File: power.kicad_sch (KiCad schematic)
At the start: 37 parts, among them Q2 BSS138-7-F, Q3 BSS138-7-F, U1 TPS56C230, U6 74AUP2G132

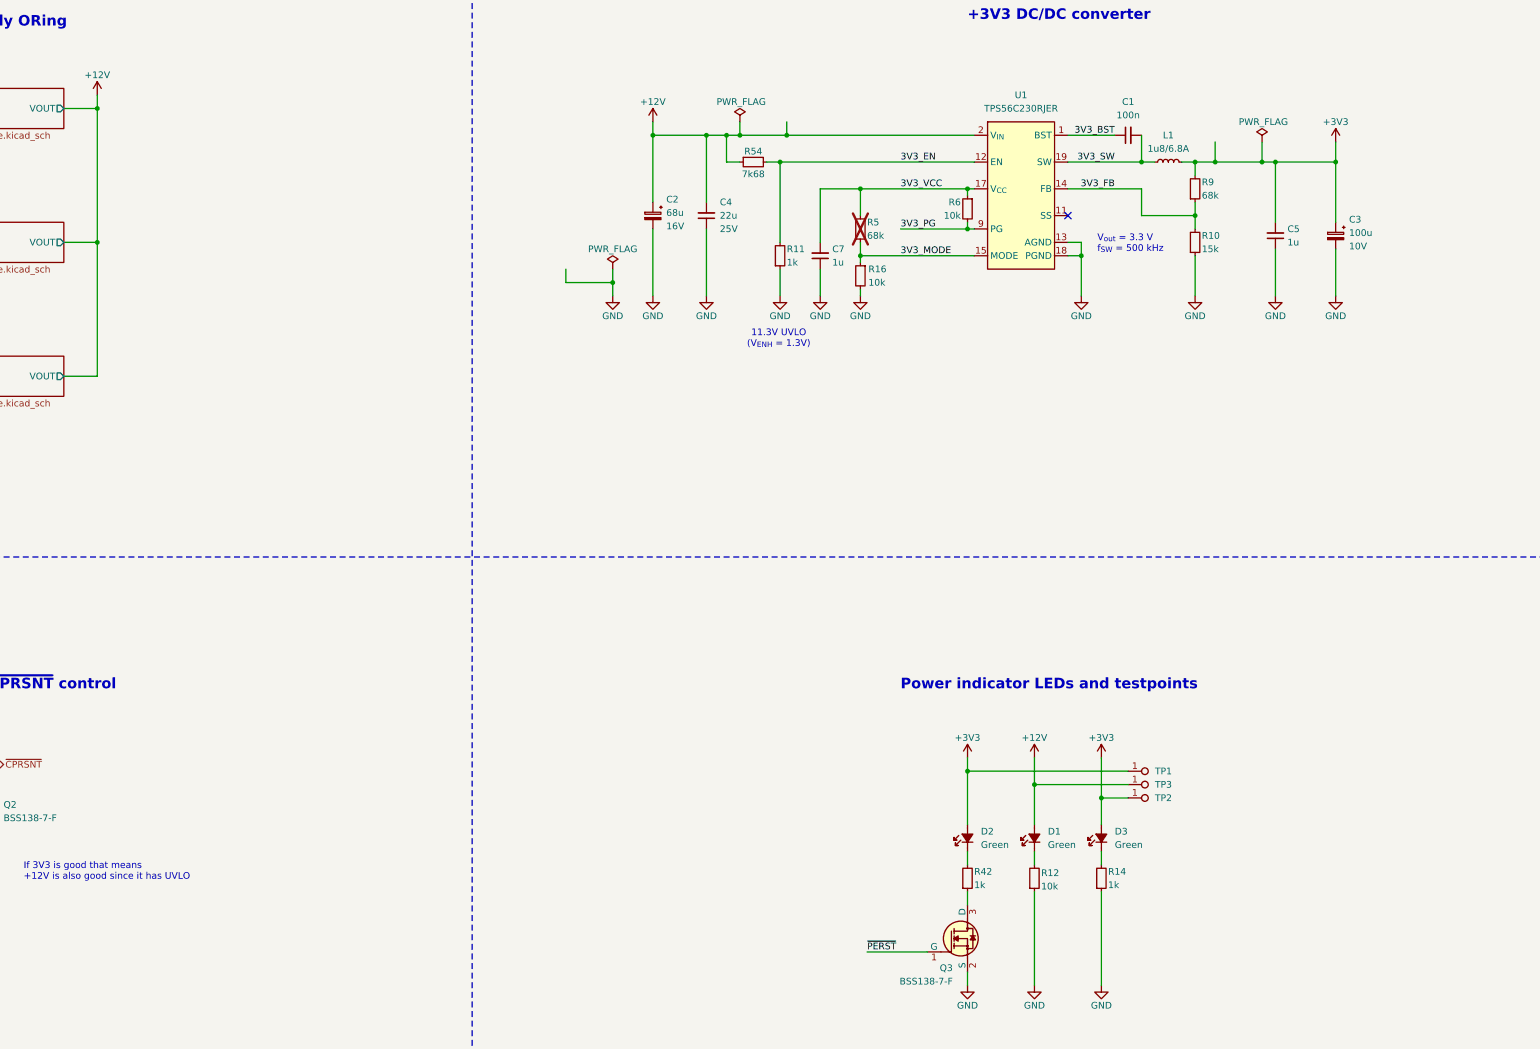
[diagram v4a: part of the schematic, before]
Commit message: [#79262] Route high speed and power
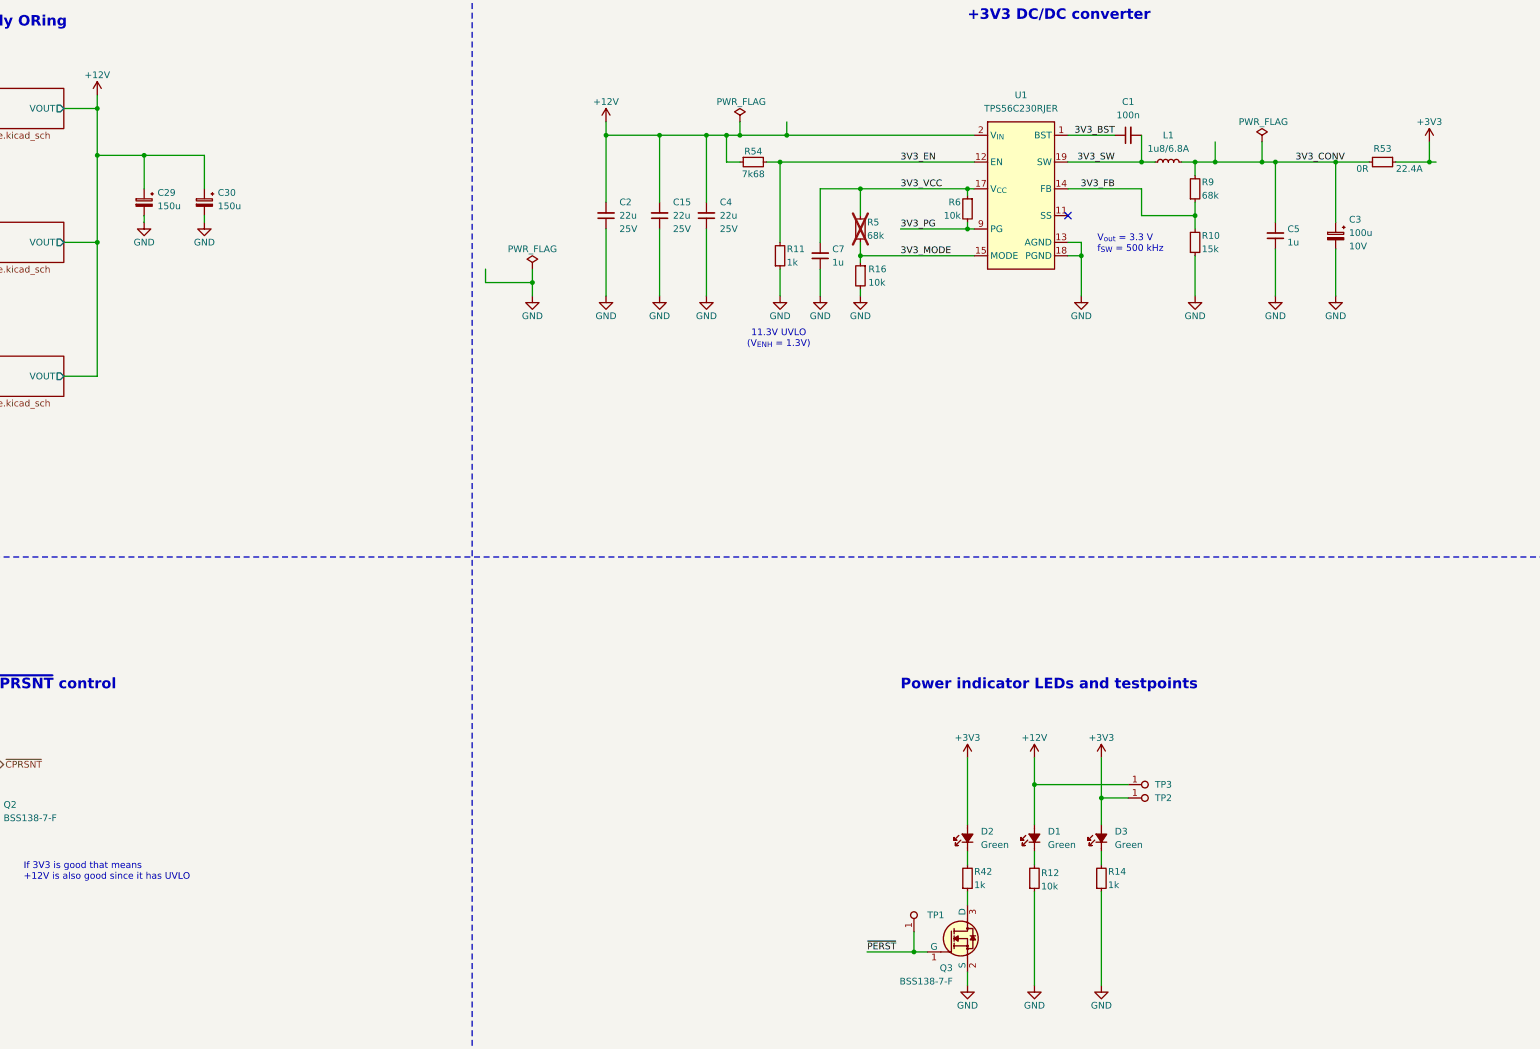
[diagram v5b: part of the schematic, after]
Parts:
- removed C2: C_Pol_68u_16V_Panasonic-TQC-D, antmicro-footprints:C_Pol_EIA-D, symbol antmicroCapacitorspol:C_Pol_68u_16V_Panasonic-TQC-D
- added C15, C2: C_22u_25V_0805, antmicro-footprints:C_0805_2012Metric, symbol antmicroCapacitorsmisc:C_22u_25V_0805
- added C29, C30: C_Pol_150u_30V_Vishay-T59-EE, antmicro-footprints:C_Pol_Vishay-T59-EE, symbol antmicroCapacitorspol:C_Pol_150u_30V_Vishay-T59-EE
- added R53: R_0R_22.4A_0603, antmicro-footprints:R_0603_1608Metric, symbol antmicroResistors0603:R_0R_22.4A_0603
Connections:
- net +12V: now also C15.2, C2.2, C29.1, C30.1
- net +3V3: now also R53.1; no longer C3.1, C5.2, L1.2, R9.2, TP1.1
- net GND: now also C15.1, C2.1, C29.2, C30.2
- net ~{PERST}: now also TP1.1
- new net 3V3_CONV: C3.1, C5.2, L1.2, R53.2, R9.2
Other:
- moved on the sheet: TP1

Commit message: [#79262] DRC clean
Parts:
- added TP7: TP_0.75mm_SMD, antmicro-footprints:TP_SMD_0.75mm, symbol antmicroTestPoints:TP_0.75mm_SMD
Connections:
- net 3V3_CONV: now also TP7.1

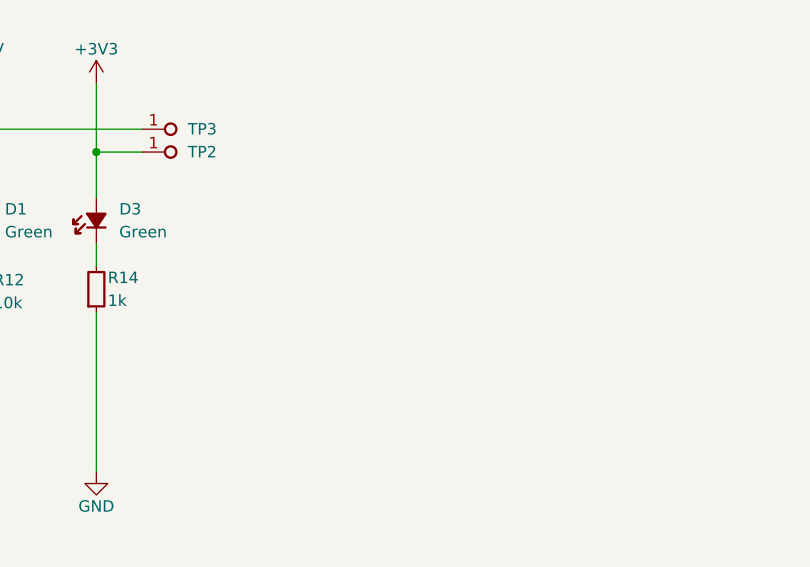
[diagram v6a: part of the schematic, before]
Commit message: [#79790] Finalized rerouting
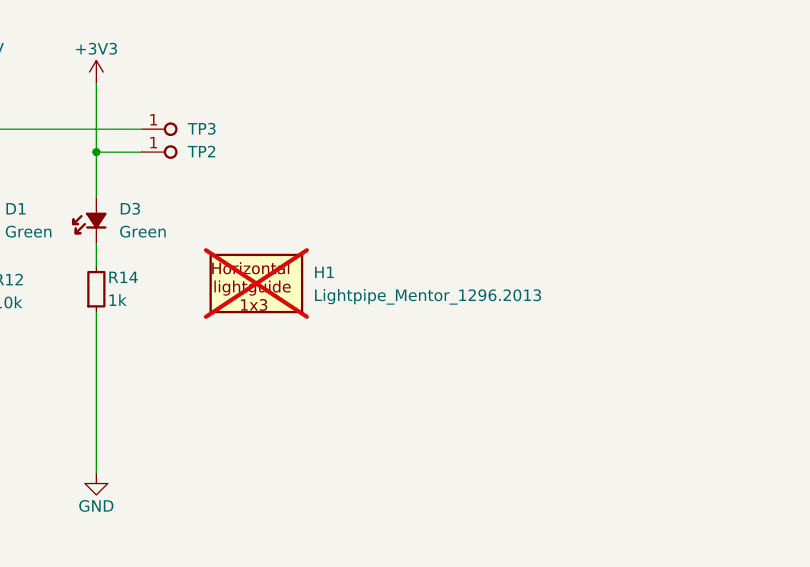
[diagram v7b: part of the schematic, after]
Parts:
- added H1: Lightpipe_Mentor_1296.2013, antmicro-footprints:Mech_Lightpipe_Mentor_1296.2013, symbol antmicroMechanicalParts:Lightpipe_Mentor_1296.2013
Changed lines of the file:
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@@
+	)
+	(symbol
+		(lib_id "antmicroMechanicalParts:Lightpipe_Mentor_1296.2013")
+		(at 335.28 213.36 0)
+		(unit 1)
+		(exclude_from_sim no)
+		(in_bom yes)
+		(on_board yes)
+		(dnp yes)
+		(fields_autoplaced yes)
+		(property "Reference" "H1"
+			(at 341.63 211.5377 0)
+			(effects
+				(font
+					(size 1.27 1.27)
+					(thickness 0.15)
+				)
+				(justify left)
+			)
+		)
+		(property "Value" "Lightpipe_Mentor_1296.2013"
+			(at 341.63 214.0777 0)
+			(effects
+				(font
+					(size 1.27 1.27)
+					(thickness 0.15)
+				)
+				(justify left)
+			)
+		)
+		(property "Footprint" "antmicro-footprints:Mech_Lightpipe_Mentor_1296.2013"
+			(at 355.6 220.98 0)
+			(effects
+				(font
+					(size 1.27 1.27)
+					(thickness 0.15)
+				)
+				(justify left bottom)
+				(hide yes)
+			)
+		)
+		(property "Datasheet" "https://docs.rs-online.com/e47b/0900766b813f6efb.pdf"
+			(at 355.6 223.52 0)
+			(effects
+				(font
+					(size 1.27 1.27)
+					(thickness 0.15)
+				)
+				(justify left bottom)
+				(hide yes)
+			)
+		)
+		(property "Description" "Light Pipe, Miniature Triple Line, 14.45 mm, 3 Pipes, Circular, PC Board, Transparent"
+			(at 335.28 213.36 0)
+			(effects
+				(font
+					(size 1.27 1.27)
+				)
+				(hide yes)
+			)
+		)
+		(property "Manufacturer" "Mentor Worldwide"
+			(at 355.6 226.06 0)
+			(effects
+				(font
+					(size 1.27 1.27)
+					(thickness 0.15)
+				)
+				(justify left bottom)
+				(hide yes)
+			)
+		)
+		(property "MPN" "1296.2013"
+			(at 355.6 228.6 0)
+			(effects
+				(font
+					(size 1.27 1.27)
+					(thickness 0.15)
+				)
+				(justify left bottom)
+				(hide yes)
+			)
+		)
+		(property "Author" "Antmicro"
+			(at 355.6 231.14 0)
+			(effects
+				(font
+					(size 1.27 1.27)
+					(thickness 0.15)
+				)
+				(justify left bottom)
+				(hide yes)
+			)
+		)
+		(property "License" "Apache-2.0"
+			(at 355.6 233.68 0)
+			(effects
+				(font
+					(size 1.27 1.27)
+					(thickness 0.15)
+				)
+				(justify left bottom)
+				(hide yes)
+			)
+		)
+		(instances
+			(project ""
+				(path "/44c3be85-0a18-4d93-a9a5-650ee09b6032/38f25804-42b6-4fac-b87c-d8c0064ff23c"
+					(reference "H1")
+					(unit 1)
+				)
+			)
+		)
 	)
 	(symbol

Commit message: [#79790] Added fiducials and double sided test points
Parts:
- TP1, TP2, TP3, TP7: value TP_0.75mm_SMD -> TP_Pad0.75mm_Drill0.2mm; footprint antmicro-footprints:TP_SMD_0.75mm -> antmicro-footprints:TP_Pad0.75mm_Drill0.2mm; symbol antmicroTestPoints:TP_0.75mm_SMD -> antmicroTestPoints:TP_Pad0.75mm_Drill0.2mm
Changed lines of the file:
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@@
 	)
 	(symbol
-		(lib_id "antmicroTestPoints:TP_0.75mm_SMD")
+		(lib_id "antmicroTestPoints:TP_Pad0.75mm_Drill0.2mm")
 		(at 322.58 195.58 0)
 		(unit 1)
@@
 			)
 		)
-		(property "Value" "TP_0.75mm_SMD"
+		(property "Value" "TP_Pad0.75mm_Drill0.2mm"
 			(at 332.74 199.39 0)
 			(effects
@@
 			)
 		)
-		(property "Footprint" "antmicro-footprints:TP_SMD_0.75mm"
+		(property "Footprint" "antmicro-footprints:TP_Pad0.75mm_Drill0.2mm"
 			(at 332.74 201.93 0)
 			(effects
@@
 	)
 	(symbol
-		(lib_id "antmicroTestPoints:TP_0.75mm_SMD")
+		(lib_id "antmicroTestPoints:TP_Pad0.75mm_Drill0.2mm")
 		(at 322.58 198.12 0)
 		(unit 1)
@@
 		(on_board yes)
 		(dnp no)
+		(fields_autoplaced yes)
 		(property "Reference" "TP2"
 			(at 327.66 198.12 0)
@@
 			)
 		)
-		(property "Value" "TP_0.75mm_SMD"
+		(property "Value" "TP_Pad0.75mm_Drill0.2mm"
 			(at 332.74 201.93 0)
 			(effects
@@
 			)
 		)
-		(property "Footprint" "antmicro-footprints:TP_SMD_0.75mm"
+		(property "Footprint" "antmicro-footprints:TP_Pad0.75mm_Drill0.2mm"
 			(at 332.74 204.47 0)
 			(effects
@@
 	)
 	(symbol
-		(lib_id "antmicroTestPoints:TP_0.75mm_SMD")
+		(lib_id "antmicroTestPoints:TP_Pad0.75mm_Drill0.2mm")
 		(at 281.94 223.52 90)
 		(unit 1)
@@
 			)
 		)
-		(property "Value" "TP_0.75mm_SMD"
+		(property "Value" "TP_Pad0.75mm_Drill0.2mm"
 			(at 285.75 213.36 0)
 			(effects
@@
 			)
 		)
-		(property "Footprint" "antmicro-footprints:TP_SMD_0.75mm"
+		(property "Footprint" "antmicro-footprints:TP_Pad0.75mm_Drill0.2mm"
 			(at 288.29 213.36 0)
 			(effects
@@
 	)
 	(symbol
-		(lib_id "antmicroTestPoints:TP_0.75mm_SMD")
+		(lib_id "antmicroTestPoints:TP_Pad0.75mm_Drill0.2mm")
 		(at 363.22 82.55 0)
 		(unit 1)
@@
 			)
 		)
-		(property "Value" "TP_0.75mm_SMD"
+		(property "Value" "TP_Pad0.75mm_Drill0.2mm"
 			(at 373.38 86.36 0)
 			(effects
@@
 			)
 		)
-		(property "Footprint" "antmicro-footprints:TP_SMD_0.75mm"
+		(property "Footprint" "antmicro-footprints:TP_Pad0.75mm_Drill0.2mm"
 			(at 373.38 88.9 0)
 			(effects
